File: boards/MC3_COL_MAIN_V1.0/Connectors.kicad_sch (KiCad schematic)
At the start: 10 parts, among them J3 ENC_leaf1, J4 ENC_leaf2, J5 ENC_leaf3, J6 ENC_leaf4

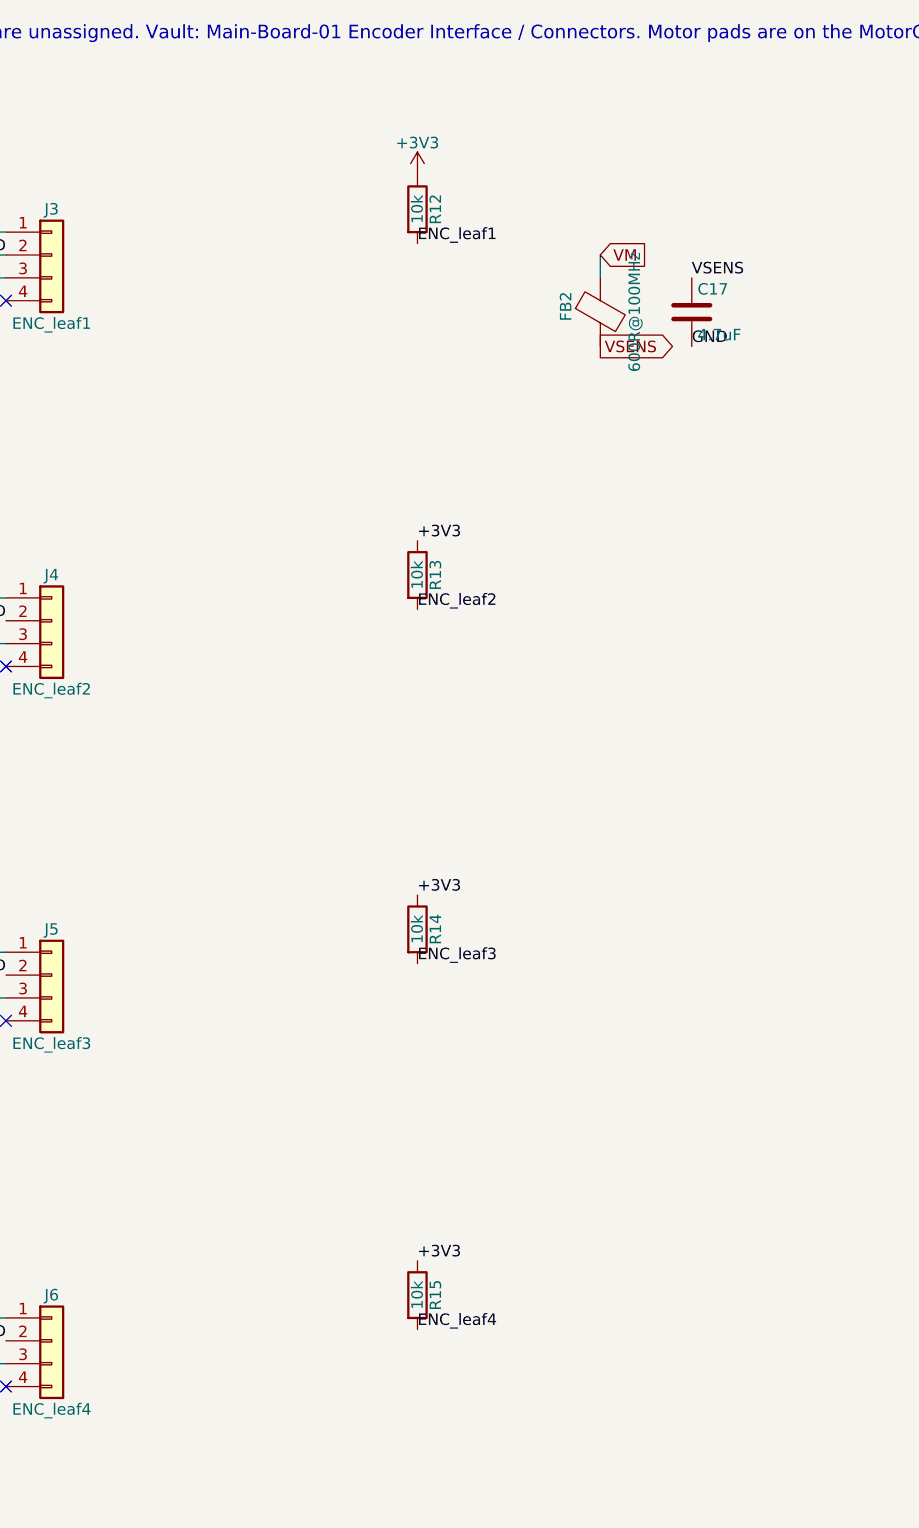
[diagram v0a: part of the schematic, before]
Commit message: V1.0: final 5 V-input state before the V1.1 fork (user board session: pixels placed, silk moves, FFC model update)
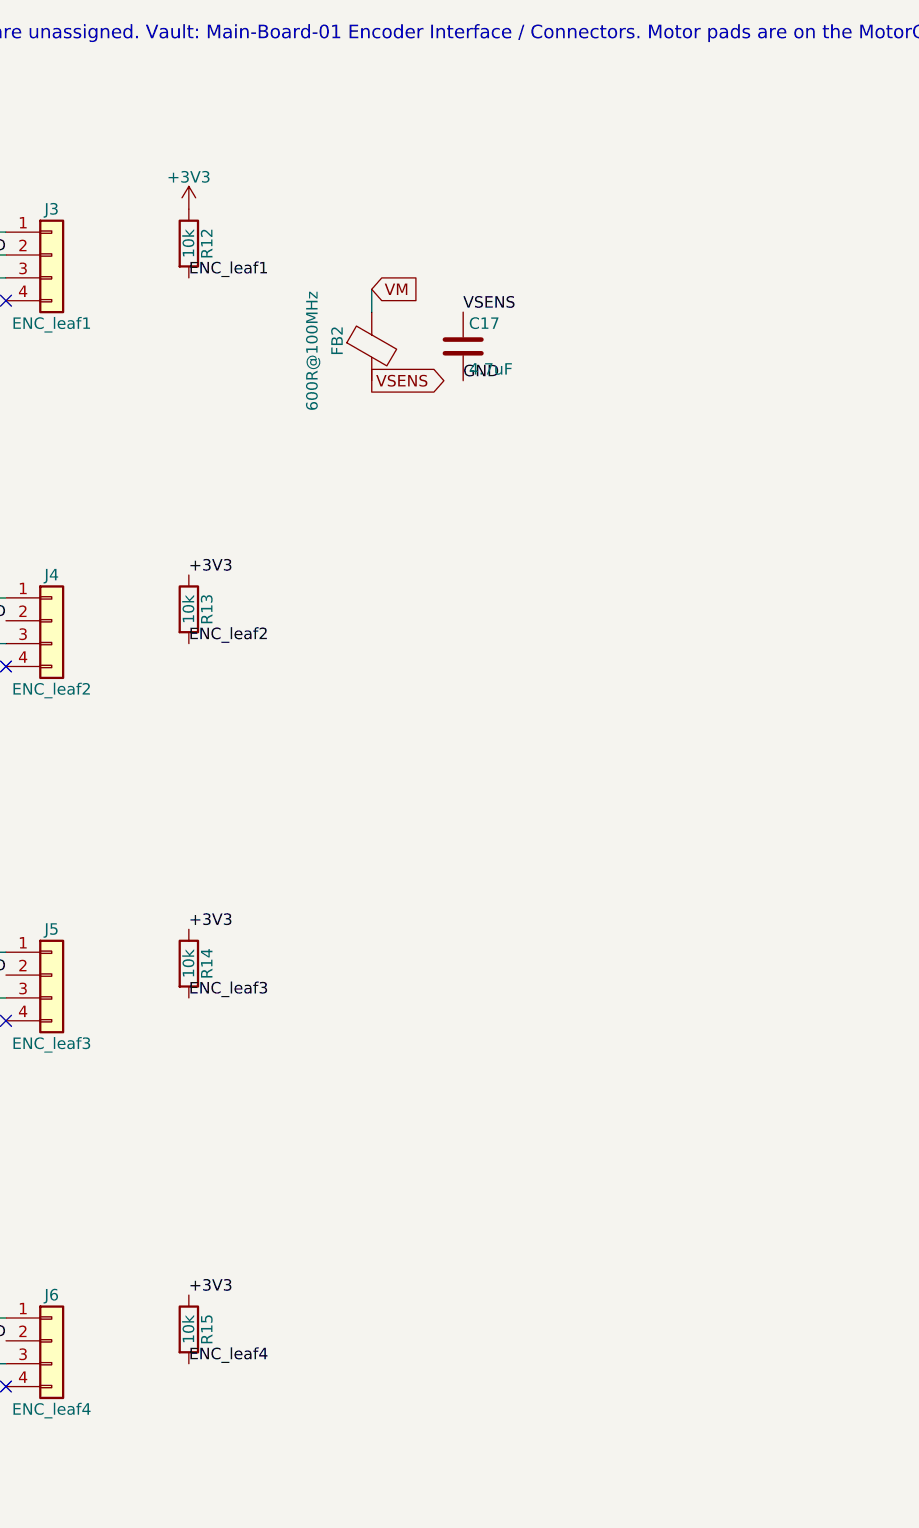
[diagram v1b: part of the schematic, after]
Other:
- moved on the sheet: C17, FB2, R12, R13, R14, R15
